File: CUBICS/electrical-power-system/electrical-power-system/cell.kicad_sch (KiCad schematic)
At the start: 9 parts, among them Q501 NMOS, Q502 NMOS, U502 BQ297xy

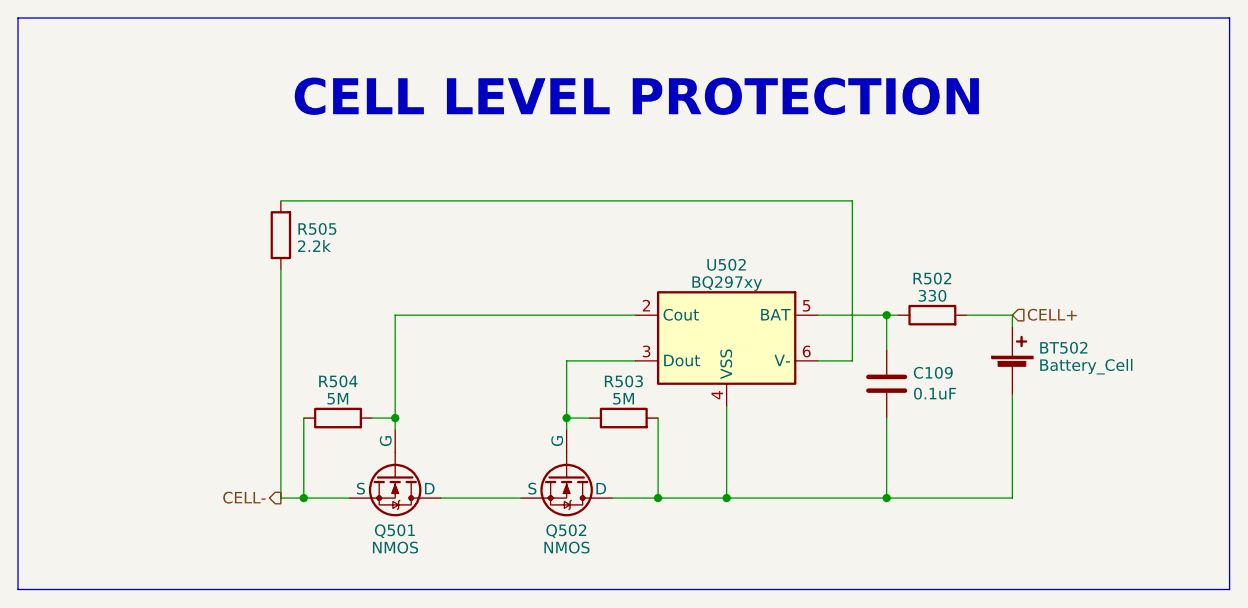
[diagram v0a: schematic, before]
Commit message: rev 1.0 routing complete updated schematic
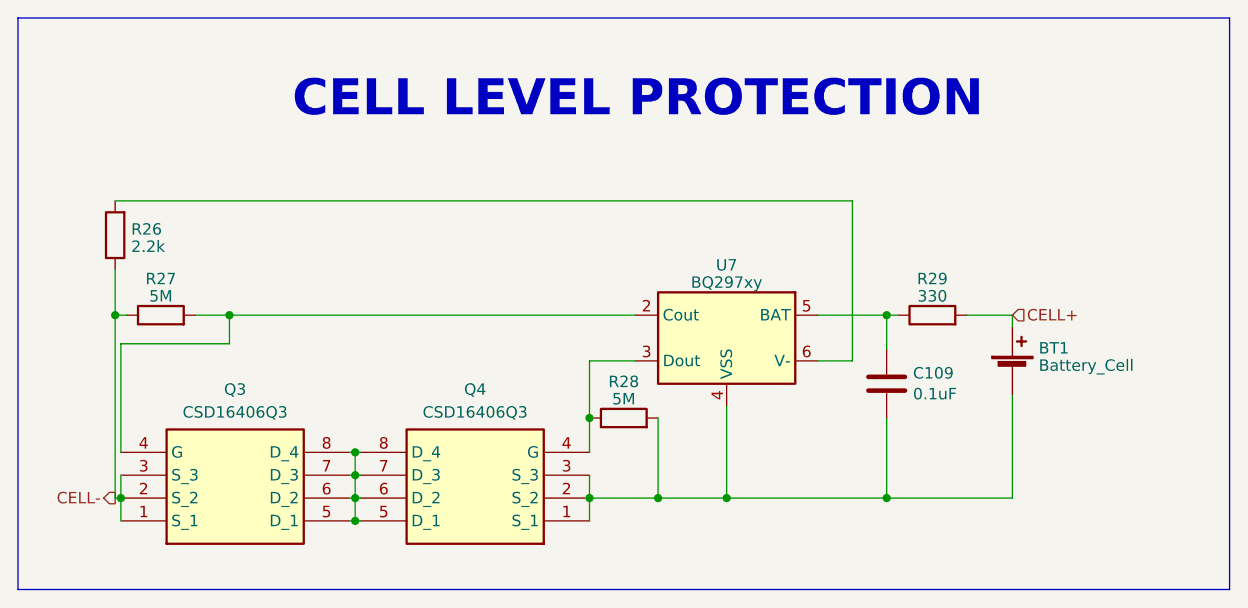
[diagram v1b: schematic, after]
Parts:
- removed Q501, Q502: NMOS, symbol Simulation_SPICE:NMOS
- added Q3, Q4: CSD16406Q3, SamacSys_Parts:DQG_VSON-CLIP, symbol SamacSys_Parts:CSD16406Q3
- BT1: renamed from BT502; footprint (none) -> footprints:18650_TH
- C109: footprint Capacitor_SMD:C_0805_2012Metric_Pad1.18x1.45mm_HandSolder -> Capacitor_SMD:C_0603_1608Metric
- R26: renamed from R505; footprint (none) -> Resistor_SMD:R_0603_1608Metric
- R27: renamed from R504; footprint (none) -> Resistor_SMD:R_0603_1608Metric
- R28: renamed from R503; footprint (none) -> Resistor_SMD:R_0603_1608Metric
- R29: renamed from R502; footprint (none) -> Resistor_SMD:R_0603_1608Metric
- renumbered U502 to U7
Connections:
- net CELL-: now also Q3.1 (S_1), Q3.2 (S_2), Q3.3 (S_3)
- net at R28.1, U7.3 (Dout): now also Q4.4 (G)
- net at BT1.2 (-), C109.2, R28.2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: now also Q4.1 (S_1), Q4.2 (S_2), Q4.3 (S_3)
- net at R27.2, U7.2 (Cout): now also Q3.4 (G)
- new net: Q3.5 (D_1), Q3.6 (D_2), Q3.7 (D_3), Q3.8 (D_4), Q4.5 (D_1), Q4.6 (D_2), Q4.7 (D_3), Q4.8 (D_4)
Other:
- moved on the sheet: R26, R27
